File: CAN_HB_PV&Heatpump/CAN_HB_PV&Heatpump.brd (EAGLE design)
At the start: 100 x 80.1 mm, 58 parts, among them IC1 ULN2003AD, IC2 PCA82C250T, IC3 7805L, Q1 4.00000

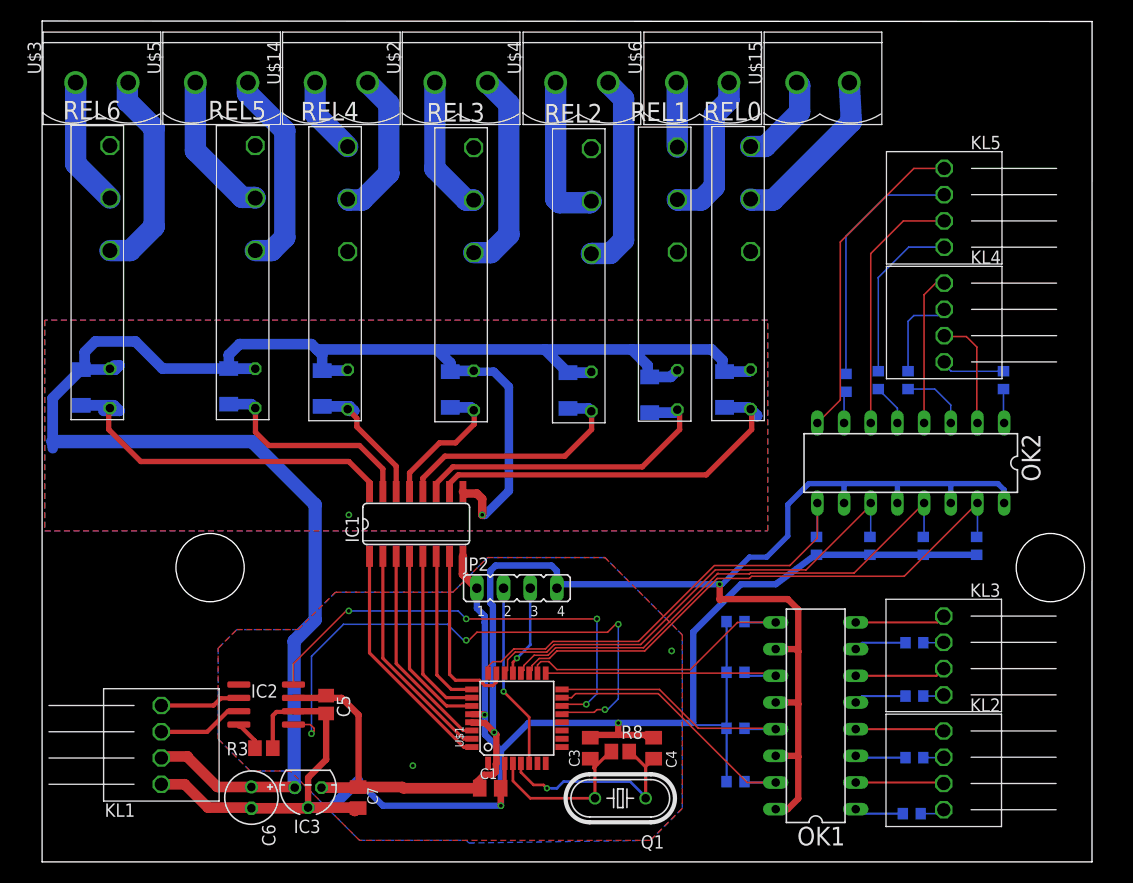
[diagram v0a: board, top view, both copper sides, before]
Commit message: 
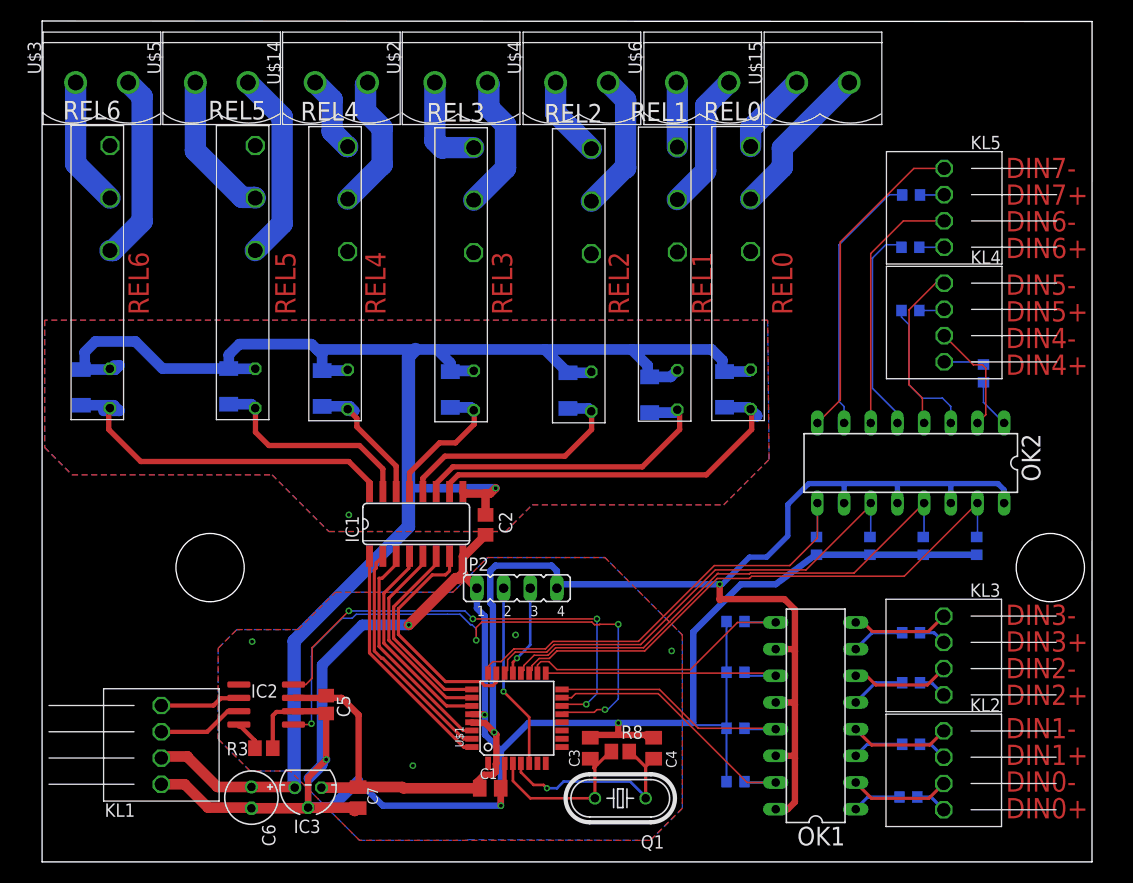
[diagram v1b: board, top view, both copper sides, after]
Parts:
- added C2: 100nF, rcl:C0805
- moved R18 18.9 mm to (82.7, 63.5), turned to 0 degrees
- moved R16 13.0 mm to (82.7, 58.5), turned to 0 degrees
- moved R14 6.64 mm to (82.7, 52.5), turned to 0 degrees
- moved R12 2.01 mm to (89.6, 46.5)
- moved R2 1.62 mm to (82.5, 6.16)
- moved R5 1.31 mm to (82.7, 11.2)
- moved R7 1.31 mm to (82.7, 17.0)
- moved R10 1.00 mm to (82.7, 21.8)
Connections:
- net CAN_RX renamed RXCAN
- net CAN_TX renamed TXCAN
- net N$1 renamed DIN0+
- net N$21 renamed DIN0-
- net N$22 renamed DIN1+
- net N$24 renamed DIN1-
- net N$25 renamed DIN2+
- net N$27 renamed DIN2-
- net N$29 renamed DIN3-
- net N$30 renamed DIN3+
- net N$31 renamed DIN4+
- net N$33 renamed DIN4-
- net N$39 renamed DIN5-
- net N$40 renamed DIN5+
- net N$41 renamed DIN6+
- net N$43 renamed DIN6-
- net N$45 renamed DIN7-
- net N$46 renamed DIN7+
- removed net CH1: REL3.12, U$2.P$2
- removed net N$18: REL2.11, U$4.P$1
- removed net N$19: REL2.12, U$4.P$2
- new net N$1: REL3.11, U$2.2
- new net N$5: REL3.14, U$2.1
- new net N$6: REL2.14, U$4.1
- net +12V: now also C2.1
- net CH4: now also U$5.2; no longer U$5.P$2
- net GND: now also C2.2
- net N$11: now also U$14.2; no longer U$14.P$2
- net N$12: now also U$14.1; no longer U$14.P$1
- net N$13: now also U$6.2; no longer U$6.P$2
- net N$14: now also U$6.1; no longer U$6.P$1
- net N$15: now also U$15.2; no longer U$15.P$2
- net N$16: now also U$15.1; no longer U$15.P$1
- net N$17: now also U$5.1; no longer U$5.P$1
- net N$20: now also U$3.2; no longer U$3.P$2
- net N$4: now also U$3.1; no longer U$3.P$1
- net N$7: now also REL2.11, U$4.2; no longer REL3.11, U$2.P$1
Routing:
- net GND: track 173.1 -> 207.9 mm, vias 5 -> 9
- net +12V: track 199.5 -> 172.6 mm
- net N$44: track 3.05 -> 25.2 mm
- net DIN7+: track 24.1 -> 2.31 mm
- net CH1: track 19.4 -> 0.00 mm
- net N$19: track 19.2 -> 0.00 mm
- net N$42: track 3.99 -> 20.1 mm
- net N$18: track 14.7 -> 0.00 mm
- net DIN6+: track 16.6 -> 2.37 mm
- net N$1: track 0.00 -> 13.2 mm
- net N$5: track 0.00 -> 9.55 mm
- net N$6: track 0.00 -> 7.71 mm
- net N$38: track 6.40 -> 13.8 mm
- net DIN5+: track 8.67 -> 2.41 mm
- net B_REL0: track 17.1 -> 22.5 mm
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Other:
- board text added: "DIN0+"
- board text added: "DIN0-"
- board text added: "DIN1+"
- board text added: "DIN1-"
- board text added: "DIN2+"
- board text added: "DIN2-"
- board text added: "DIN3+"
- board text added: "DIN3-"
- board text added: "DIN4+"
- board text added: "DIN4-"
- board text added: "DIN5+"
- board text added: "DIN5-"
- board text added: "DIN6+"
- board text added: "DIN6-"
- board text added: "DIN7+"
- board text added: "DIN7-"
- board text added: "REL0"
- board text added: "REL1"
- board text added: "REL2"
- board text added: "REL3"
- board text added: "REL4"
- board text added: "REL5"
- board text added: "REL6"

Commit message: hardware finalized
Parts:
- R1, R10, R11, R12, R13, R14, R15, R16, R17, R18, R4, R6, R7, R9: device rcl:R0603 -> rcl:R0805
- R2, R5: value (none) -> 10k; device rcl:R0603 -> rcl:R0805
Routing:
- net GND: track 207.9 -> 197.0 mm
- net TXCAN: track 55.7 -> 51.4 mm
- net +12V: track 172.6 -> 171.0 mm
- net DIN4: track 52.9 -> 53.4 mm

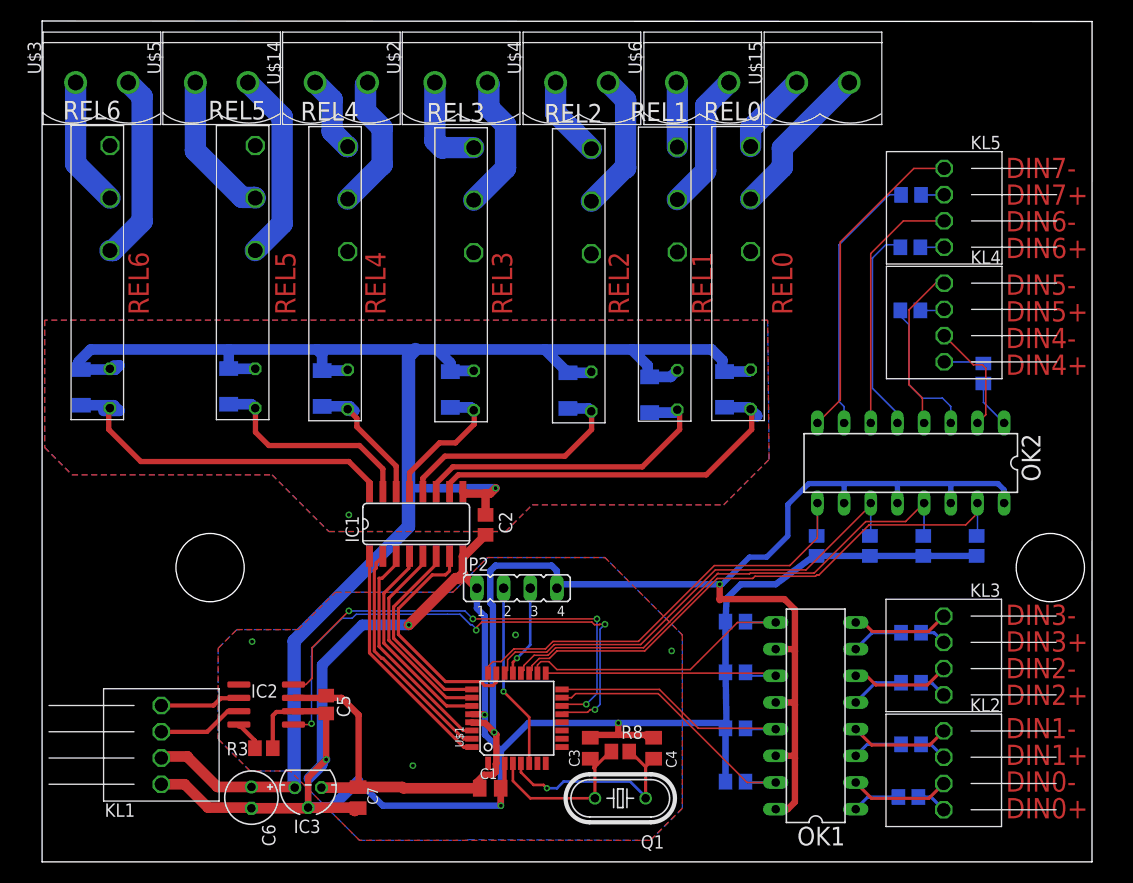
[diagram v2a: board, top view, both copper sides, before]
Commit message: PV_Heatpump Wiring plan added Firmware setup done
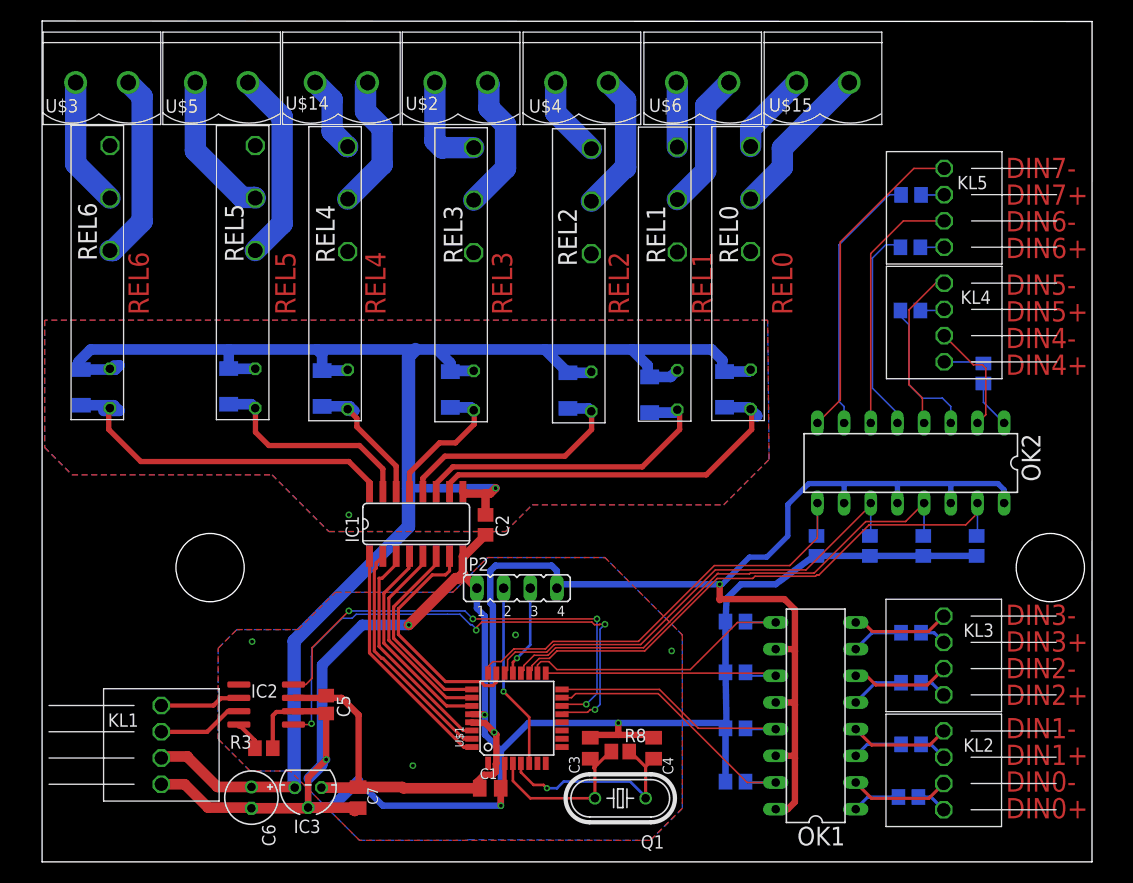
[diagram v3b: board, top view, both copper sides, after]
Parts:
- R10, R12, R14, R16, R18, R7: value (none) -> 10k
